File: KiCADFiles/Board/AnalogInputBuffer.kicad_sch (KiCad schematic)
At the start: 18 parts, among them U15 OPA1655D, U16 OPA1655D

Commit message: chose all components
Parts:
- removed RV1: RL_5K, symbol Device:R_Potentiometer
- added RV4: 5k, Potentiometer_THT:Potentiometer_Alps_RK163_Single_Horizontal, symbol Device:R_Potentiometer
- C43: value 10uF -> 10u; footprint ~ -> PCM_SparkFun-Capacitor:C_0805_2012Metric; MPN (none) -> CL21A106KAYNNNG; Voltage (none) -> 25V
- C44: footprint ~ -> PCM_SparkFun-Capacitor:C_0603_1608Metric; MPN (none) -> CL10B104KB8NNNL
- C80: value 100p -> 0.1u; footprint ~ -> PCM_SparkFun-Capacitor:C_0603_1608Metric; MPN (none) -> CL10B104KB8NNNL
- C81, C82: footprint ~ -> PCM_SparkFun-Capacitor:C_0603_1608Metric; MPN (none) -> GRM1885C1H102JA01D
- C85, C86: value 5n -> 5800p; footprint ~ -> PCM_SparkFun-Capacitor:C_0603_1608Metric; MPN (none) -> GCM1885C1H562GA16D
- FB5: value ${SIM.PARAMS} -> 220; footprint ~ -> Inductor_SMD:L_0603_1608Metric; MPN (none) -> MMZ1608B221CTAH0
- R14, R67, R69: footprint ~ -> PCM_SparkFun-Resistor:R_0805_2012Metric; MPN (none) -> ERA-6AEB102V
- R65: footprint (none) -> PCM_SparkFun-Resistor:R_0805_2012Metric; MPN (none) -> CRCW080510K0FKEA
- R70, R71: value 40 -> 34; footprint ~ -> PCM_SparkFun-Resistor:R_0805_2012Metric; MPN (none) -> CRCW080534R0FKEA
- R8: footprint ~ -> PCM_SparkFun-Resistor:R_0805_2012Metric; MPN (none) -> RMCF0805JT510R
- U15, U16: MPN (none) -> OPA1655D
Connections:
- net AMP_SIGIN+: now also RV4.3
- net at R8.1: now also RV4.1, RV4.2

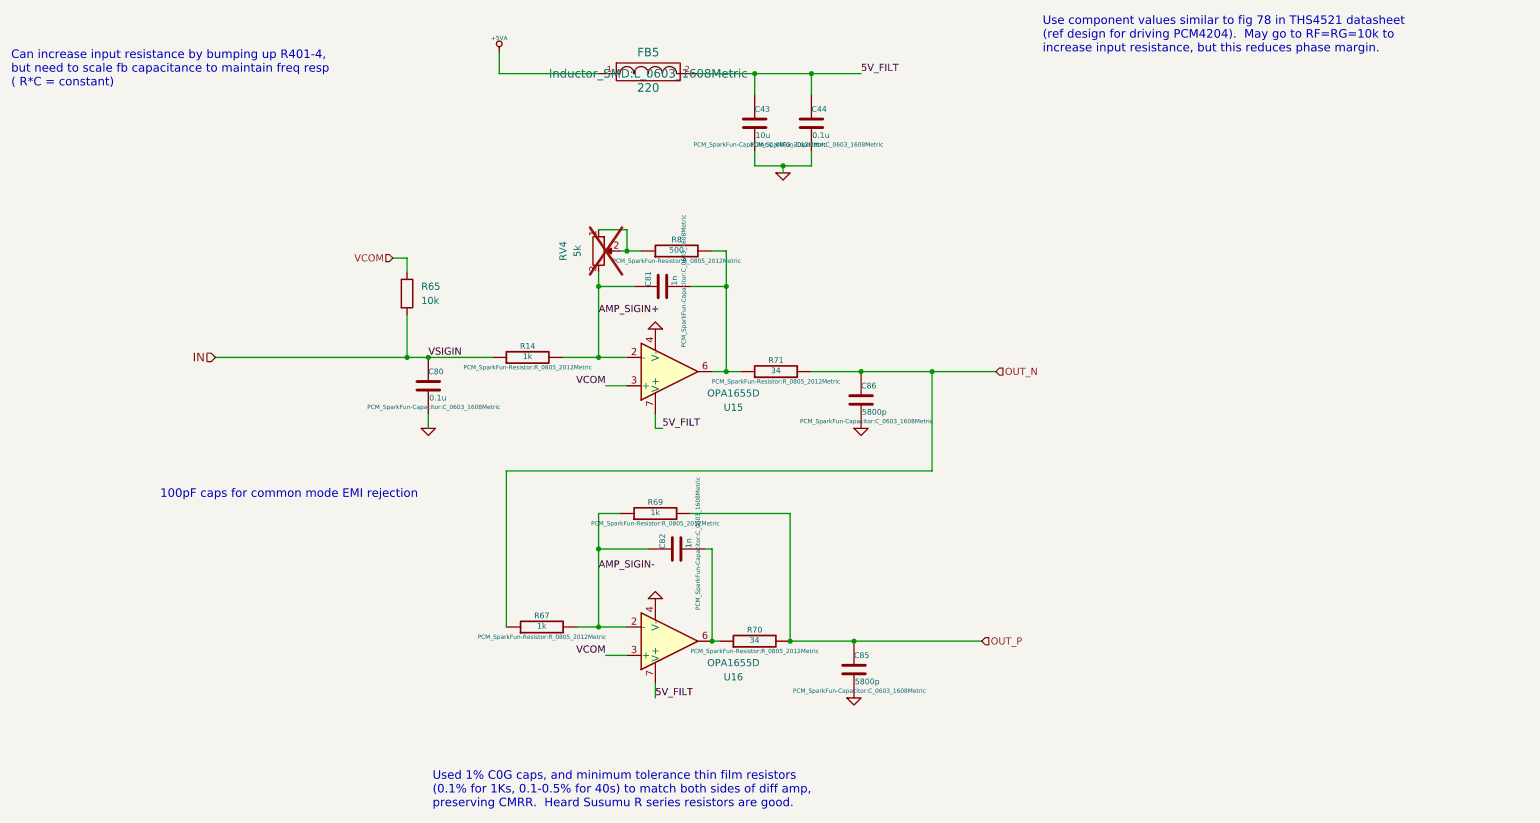
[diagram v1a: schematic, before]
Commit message: replaced sw with relay, routed line amp section
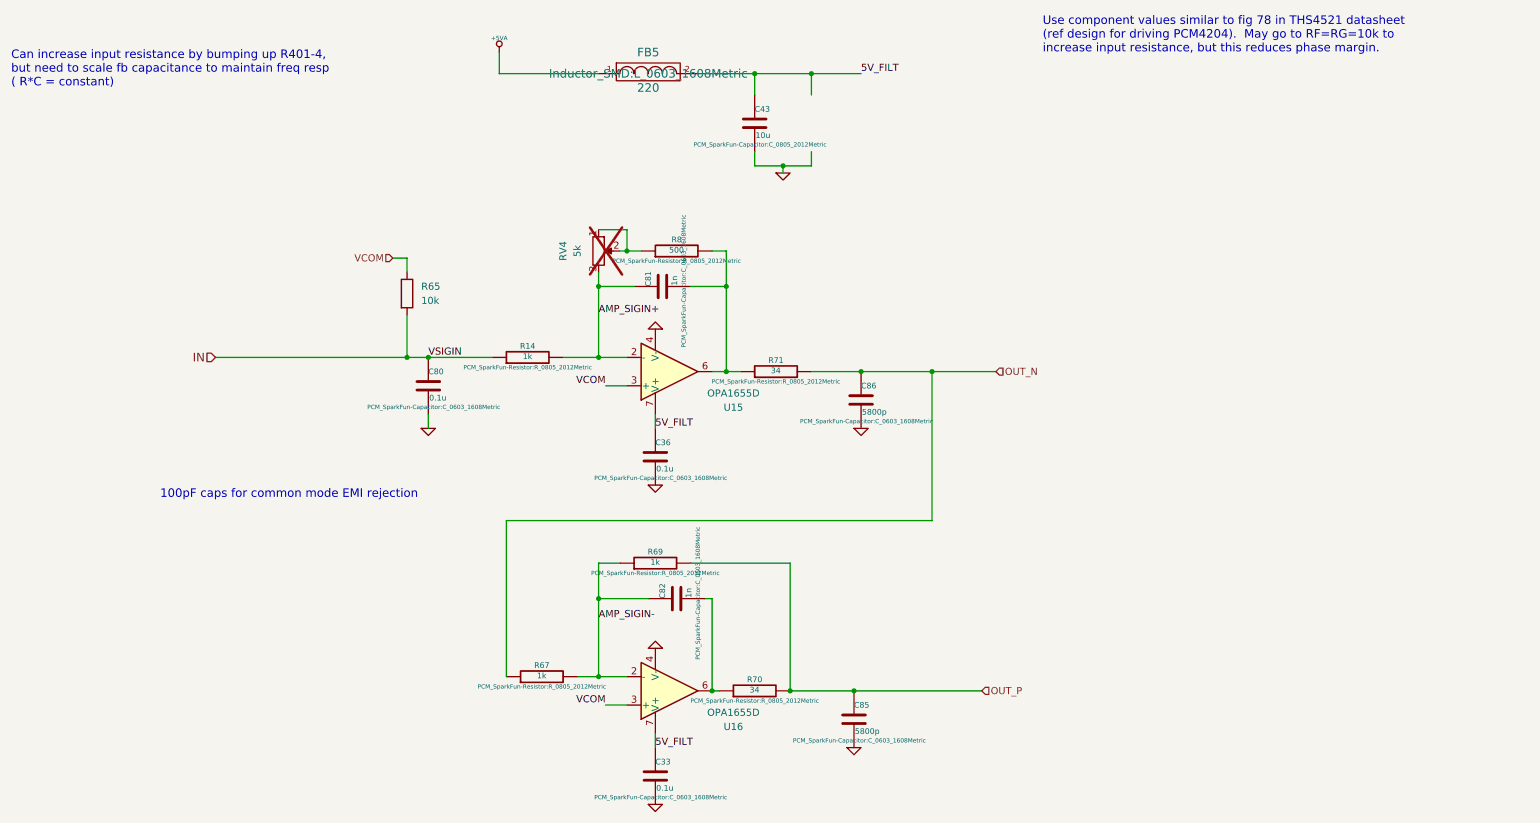
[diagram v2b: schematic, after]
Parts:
- removed C44: 0.1u, PCM_SparkFun-Capacitor:C_0603_1608Metric, symbol SuperAudioBoard-rescue:C
- added C33, C36: 0.1u, PCM_SparkFun-Capacitor:C_0603_1608Metric, symbol SuperAudioBoard-rescue:C
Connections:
- net 5V_FILT: now also C33.1, C36.1
- net GND: now also C33.2, C36.2
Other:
- note removed: "Used 1% C0G caps, and minimum tolerance thin film resistors (0.1% for 1Ks, 0.1-0.5% for 40s) to match both sides of diff amp, preserving CMRR. Heard Susumu R series resistors are good."
- moved on the sheet: C82, C85, R67, R69, R70, U16

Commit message: removed connectors and condensed layout
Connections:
- net OUT_N: now also R8.2
- net at C81.2, R71.1, U15.6: no longer R8.2

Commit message: improved layout further
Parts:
- removed RV4: 5k, Potentiometer_THT:Potentiometer_Alps_RK163_Single_Horizontal, symbol Device:R_Potentiometer
- added J8: 5k Log Pot, Connector_PinHeader_2.54mm:PinHeader_1x02_P2.54mm_Vertical, symbol Connector:Conn_01x02_Pin
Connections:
- net AMP_SIGIN+: now also J8.2 (Pin_2)
- net at R8.1: now also J8.1 (Pin_1)
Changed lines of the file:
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@@
-	)
-	(junction
-		(at 129.54 59.69)
-		(diameter 0)
-		(color 0 0 0 0)
 	)
 	(junction
@@
 	(wire
 		(pts
+			(xy 124.46 59.69) (xy 132.08 59.69)
+		)
+		(stroke
+			(width 0)
+			(type default)
+		)
+	)
+	(wire
+		(pts
 			(xy 124.46 78.74) (xy 129.54 78.74)
 		)
@@
 	(wire
 		(pts
-			(xy 124.46 55.88) (xy 129.54 55.88)
-		)
-		(stroke
-			(width 0)
-			(type default)
-		)
-	)
-	(wire
-		(pts
 			(xy 90.17 71.12) (xy 90.17 78.74)
 		)
@@
 	(wire
 		(pts
-			(xy 129.54 59.69) (xy 132.08 59.69)
-		)
-		(stroke
-			(width 0)
-			(type default)
-		)
-	)
-	(wire
-		(pts
 			(xy 158.75 115.57) (xy 158.75 138.43)
 		)
@@
 	(wire
 		(pts
-			(xy 128.27 59.69) (xy 129.54 59.69)
-		)
-		(stroke
-			(width 0)
-			(type default)
-		)
-	)
-	(wire
-		(pts
 			(xy 140.97 66.04) (xy 147.32 66.04)
 		)
@@
 	(wire
 		(pts
+			(xy 124.46 60.96) (xy 124.46 59.69)
+		)
+		(stroke
+			(width 0)
+			(type default)
+		)
+	)
+	(wire
+		(pts
 			(xy 144.78 138.43) (xy 146.05 138.43)
 		)
@@
 		(pts
 			(xy 125.73 140.97) (xy 129.54 140.97)
-		)
-		(stroke
-			(width 0)
-			(type default)
-		)
-	)
-	(wire
-		(pts
-			(xy 129.54 55.88) (xy 129.54 59.69)
 		)
 		(stroke
@@
 	)
 	(symbol
-		(lib_id "Device:R_Potentiometer")
-		(at 124.46 59.69 0)
-		(unit 1)
-		(exclude_from_sim no)
-		(in_bom yes)
-		(on_board yes)
-		(dnp yes)
-		(property "Reference" "RV4"
-			(at 118.11 59.69 90)
-			(effects
-				(font
-					(size 1.27 1.27)
-				)
-			)
-		)
-		(property "Value" "5k"
-			(at 120.65 59.69 90)
-			(effects
-				(font
-					(size 1.27 1.27)
-				)
-			)
-		)
-		(property "Footprint" "Potentiometer_THT:Potentiometer_Alps_RK163_Single_Horizontal"
-			(at 124.46 59.69 0)
-			(effects
-				(font
-					(size 1.27 1.27)
-				)
-				(hide yes)
-			)
-		)
-		(property "Datasheet" "~"
-			(at 124.46 59.69 0)
-			(effects
-				(font
-					(size 1.27 1.27)
-				)
-				(hide yes)
-			)
-		)
-		(property "Description" "Potentiometer"
-			(at 124.46 59.69 0)
-			(effects
-				(font
-					(size 1.27 1.27)
-				)
-				(hide yes)
-			)
-		)
-		(property "MPN" "RV16AF-10-15K-C5K-3LA "
-			(at 124.46 59.69 0)
-			(effects
-				(font
-					(size 1.27 1.27)
-				)
-				(hide yes)
-			)
-		)
-		(property "Tol" ""
-			(at 124.46 59.69 0)
-			(effects
-				(font
-					(size 1.27 1.27)
-				)
-				(hide yes)
-			)
-		)
-		(pin "3"
-		)
-		(pin "2"
-		)
-		(pin "1"
-		)
-		(instances
-			(project "SuperAudioBoard"
-				(path "/01f65e03-4e05-4001-87b4-b3e88e4198ab/00000000-0000-0000-0000-00005438c479/00000000-0000-0000-0000-0000544f05bf"
-					(reference "RV4")
-					(unit 1)
-				)
-				(path "/01f65e03-4e05-4001-87b4-b3e88e4198ab/00000000-0000-0000-0000-00005438c479/00000000-0000-0000-0000-00005456b8dd"
-					(reference "RV5")
-					(unit 1)
-				)
-			)
-		)
-	)
-	(symbol
 		(lib_name "C_16")
 		(lib_id "SuperAudioBoard-rescue:C")
@@
 					(unit 1)
 				)
+			)
+		)
+	)
+	(symbol
+		(lib_id "Connector:Conn_01x02_Pin")
+		(at 119.38 60.96 0)
+		(unit 1)
+		(exclude_from_sim no)
+		(in_bom yes)
+		(on_board yes)
+		(dnp no)
+		(fields_autoplaced yes)
+		(property "Reference" "J8"
+			(at 120.015 55.88 0)
+			(effects
+				(font
+					(size 1.27 1.27)
+				)
+			)
+		)
+		(property "Value" "5k Log Pot"
+			(at 120.015 58.42 0)
+			(effects
+				(font
+					(size 1.27 1.27)
+				)
+			)
+		)
+		(property "Footprint" "Connector_PinHeader_2.54mm:PinHeader_1x02_P2.54mm_Vertical"
+			(at 119.38 60.96 0)
+			(effects
+				(font
+					(size 1.27 1.27)
+				)
+				(hide yes)
+			)
+		)
+		(property "Datasheet" "~"
+			(at 119.38 60.96 0)
+			(effects
+				(font
+					(size 1.27 1.27)
+				)
+				(hide yes)
+			)
+		)
+		(property "Description" "Generic connector, single row, 01x02, script generated"
+			(at 119.38 60.96 0)
+			(effects
+				(font
+					(size 1.27 1.27)
+				)
+				(hide yes)
+			)
+		)
+		(property "MPN" "RV16AF-10-15K-C5K-3LA "
+			(at 119.38 60.96 0)
+			(effects
+				(font
+					(size 1.27 1.27)
+				)
+				(hide yes)
+			)
+		)
+		(pin "2"
+		)
+		(pin "1"
+		)
+		(instances
+			(project ""
+				(path "/01f65e03-4e05-4001-87b4-b3e88e4198ab/00000000-0000-0000-0000-00005438c479/00000000-0000-0000-0000-0000544f05bf"
+					(reference "J8")
+					(unit 1)
+				)
+				(path "/01f65e03-4e05-4001-87b4-b3e88e4198ab/00000000-0000-0000-0000-00005438c479/00000000-0000-0000-0000-00005456b8dd"
+					(reference "J9")
+					(unit 1)
+				)

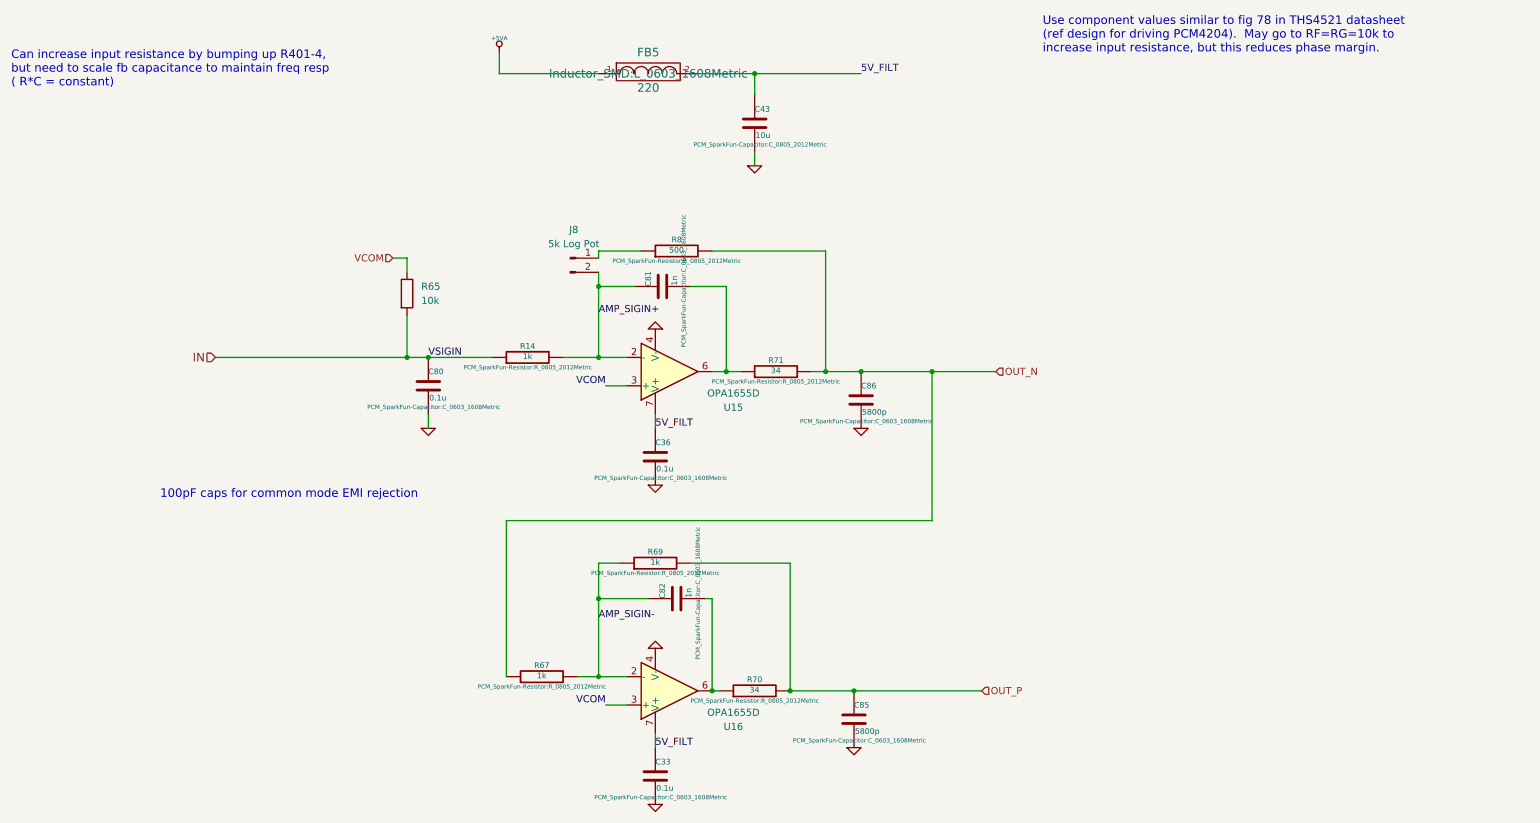
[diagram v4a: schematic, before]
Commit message: finished layout, passed DRC
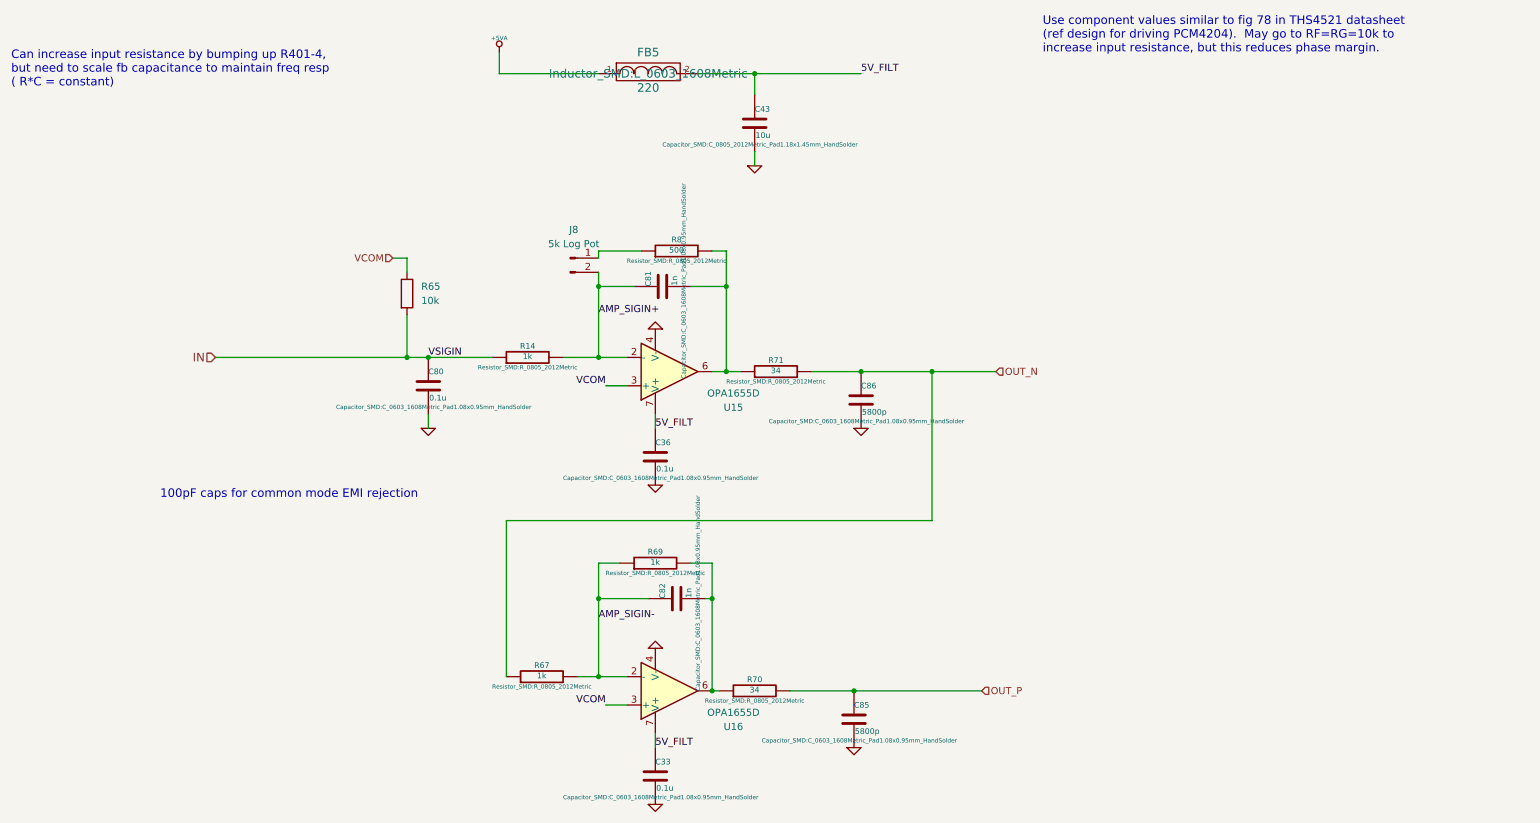
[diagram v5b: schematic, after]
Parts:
- C33, C36, C80, C81, C82, C85, C86: footprint PCM_SparkFun-Capacitor:C_0603_1608Metric -> Capacitor_SMD:C_0603_1608Metric_Pad1.08x0.95mm_HandSolder
- C43: footprint PCM_SparkFun-Capacitor:C_0805_2012Metric -> Capacitor_SMD:C_0805_2012Metric_Pad1.18x1.45mm_HandSolder
- R14, R65, R67, R69, R70, R71, R8: footprint PCM_SparkFun-Resistor:R_0805_2012Metric -> Resistor_SMD:R_0805_2012Metric
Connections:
- net OUT_N: no longer R8.2
- net OUT_P: no longer R69.2
- net at C81.2, R71.1, U15.6: now also R8.2
- net at C82.2, R70.1, U16.6: now also R69.2
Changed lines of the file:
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@@
 	)
 	(junction
-		(at 170.18 138.43)
-		(diameter 0)
-		(color 0 0 0 0)
-	)
-	(junction
-		(at 124.46 121.92)
+		(at 144.78 121.92)
 		(diameter 0)
 		(color 0 0 0 0)
 	)
 	(junction
-		(at 184.15 81.28)
+		(at 170.18 138.43)
 		(diameter 0)
 		(color 0 0 0 0)
 	)
 	(junction
-		(at 147.32 81.28)
+		(at 124.46 121.92)
 		(diameter 0)
 		(color 0 0 0 0)
 	)
 	(junction
-		(at 158.75 138.43)
+		(at 184.15 81.28)
 		(diameter 0)
 		(color 0 0 0 0)
 	)
 	(junction
-		(at 165.1 81.28)
+		(at 147.32 81.28)
 		(diameter 0)
 		(color 0 0 0 0)
@@
 	)
 	(junction
+		(at 147.32 66.04)
+		(diameter 0)
+		(color 0 0 0 0)
+	)
+	(junction
 		(at 124.46 78.74)
 		(diameter 0)
@@
 	(wire
 		(pts
-			(xy 171.45 81.28) (xy 184.15 81.28)
+			(xy 147.32 59.69) (xy 147.32 66.04)
 		)
 		(stroke
@@
 	(wire
 		(pts
-			(xy 158.75 115.57) (xy 158.75 138.43)
+			(xy 171.45 81.28) (xy 184.15 81.28)
 		)
 		(stroke
@@
 	(wire
 		(pts
-			(xy 144.78 59.69) (xy 165.1 59.69)
+			(xy 144.78 59.69) (xy 147.32 59.69)
 		)
 		(stroke
@@
 	(wire
 		(pts
-			(xy 140.97 115.57) (xy 158.75 115.57)
-		)
-		(stroke
-			(width 0)
-			(type default)
-		)
-	)
-	(wire
-		(pts
 			(xy 124.46 63.5) (xy 124.46 66.04)
 		)
@@
 	(wire
 		(pts
-			(xy 162.56 81.28) (xy 165.1 81.28)
+			(xy 125.73 140.97) (xy 129.54 140.97)
 		)
 		(stroke
@@
 	(wire
 		(pts
-			(xy 125.73 140.97) (xy 129.54 140.97)
+			(xy 106.68 27.94) (xy 124.46 27.94)
 		)
 		(stroke
@@
 	(wire
 		(pts
-			(xy 106.68 27.94) (xy 124.46 27.94)
+			(xy 162.56 81.28) (xy 171.45 81.28)
 		)
 		(stroke
@@
 	(wire
 		(pts
-			(xy 165.1 81.28) (xy 171.45 81.28)
+			(xy 140.97 115.57) (xy 144.78 115.57)
 		)
 		(stroke
@@
 	(wire
 		(pts
-			(xy 165.1 59.69) (xy 165.1 81.28)
+			(xy 144.78 115.57) (xy 144.78 121.92)
 		)
 		(stroke
@@
 			)
 		)
-		(property "Footprint" "PCM_SparkFun-Capacitor:C_0805_2012Metric"
+		(property "Footprint" "Capacitor_SMD:C_0805_2012Metric_Pad1.18x1.45mm_HandSolder"
 			(at 153.3652 40.64 0)
 			(effects
@@
 			)
 		)
-		(property "Footprint" "PCM_SparkFun-Resistor:R_0805_2012Metric"
+		(property "Footprint" "Resistor_SMD:R_0805_2012Metric"
 			(at 88.392 67.31 90)
 			(effects
@@
 			)
 		)
-		(property "Footprint" "PCM_SparkFun-Resistor:R_0805_2012Metric"
+		(property "Footprint" "Resistor_SMD:R_0805_2012Metric"
 			(at 114.3 137.668 90)
 			(effects
@@
 			)
 		)
-		(property "Footprint" "PCM_SparkFun-Capacitor:C_0603_1608Metric"
+		(property "Footprint" "Capacitor_SMD:C_0603_1608Metric_Pad1.08x0.95mm_HandSolder"
 			(at 135.5852 100.33 0)
 			(effects
@@
 			)
 		)
-		(property "Footprint" "PCM_SparkFun-Capacitor:C_0603_1608Metric"
+		(property "Footprint" "Capacitor_SMD:C_0603_1608Metric_Pad1.08x0.95mm_HandSolder"
 			(at 135.5852 157.48 0)
 			(effects
@@
 			)
 		)
-		(property "Footprint" "PCM_SparkFun-Resistor:R_0805_2012Metric"
+		(property "Footprint" "Resistor_SMD:R_0805_2012Metric"
 			(at 111.76 80.518 90)
 			(effects
@@
 			)
 		)
-		(property "Footprint" "PCM_SparkFun-Capacitor:C_0603_1608Metric"
+		(property "Footprint" "Capacitor_SMD:C_0603_1608Metric_Pad1.08x0.95mm_HandSolder"
 			(at 139.7 65.0748 0)
 			(effects
@@
 			)
 		)
-		(property "Footprint" "PCM_SparkFun-Capacitor:C_0603_1608Metric"
+		(property "Footprint" "Capacitor_SMD:C_0603_1608Metric_Pad1.08x0.95mm_HandSolder"
 			(at 171.1452 147.32 0)
 			(effects
@@
 			)
 		)
-		(property "Footprint" "PCM_SparkFun-Resistor:R_0805_2012Metric"
+		(property "Footprint" "Resistor_SMD:R_0805_2012Metric"
 			(at 138.43 61.468 90)
 			(effects
@@
 			)
 		)
-		(property "Footprint" "PCM_SparkFun-Resistor:R_0805_2012Metric"
+		(property "Footprint" "Resistor_SMD:R_0805_2012Metric"
 			(at 152.4 140.208 90)
 			(effects
@@
 			)
 		)
-		(property "Footprint" "PCM_SparkFun-Capacitor:C_0603_1608Metric"
+		(property "Footprint" "Capacitor_SMD:C_0603_1608Metric_Pad1.08x0.95mm_HandSolder"
 			(at 142.24 120.9548 0)
 			(effects
@@
 			)
 		)
-		(property "Footprint" "PCM_SparkFun-Resistor:R_0805_2012Metric"
+		(property "Footprint" "Resistor_SMD:R_0805_2012Metric"
 			(at 156.21 83.058 90)
 			(effects
@@
 			)
 		)
-		(property "Footprint" "PCM_SparkFun-Resistor:R_0805_2012Metric"
+		(property "Footprint" "Resistor_SMD:R_0805_2012Metric"
 			(at 134.62 117.348 90)
 			(effects
@@
 			)
 		)
-		(property "Footprint" "PCM_SparkFun-Capacitor:C_0603_1608Metric"
+		(property "Footprint" "Capacitor_SMD:C_0603_1608Metric_Pad1.08x0.95mm_HandSolder"
 			(at 94.9452 87.63 0)
 			(effects
@@
 			)
 		)
-		(property "Footprint" "PCM_SparkFun-Capacitor:C_0603_1608Metric"
+		(property "Footprint" "Capacitor_SMD:C_0603_1608Metric_Pad1.08x0.95mm_HandSolder"
 			(at 172.4152 90.17 0)
 			(effects
